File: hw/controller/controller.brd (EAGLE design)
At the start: 45 x 45 mm, 76 parts, among them J1 JST-PH3SMT_VERT, J2 JST-PH3SMT_VERT, Q1 TPN1R603PL, Q2 TPN1R603PL, Q3 TPN1R603PL, Q4 TPN1R603PL, Q5 TPN1R603PL, Q6 TPN1R603PL, U1 STM32F4R_64PIN, U2 DRV8323RS, U3 AS5147, U4 MAX13431E, X1 8.0MHz

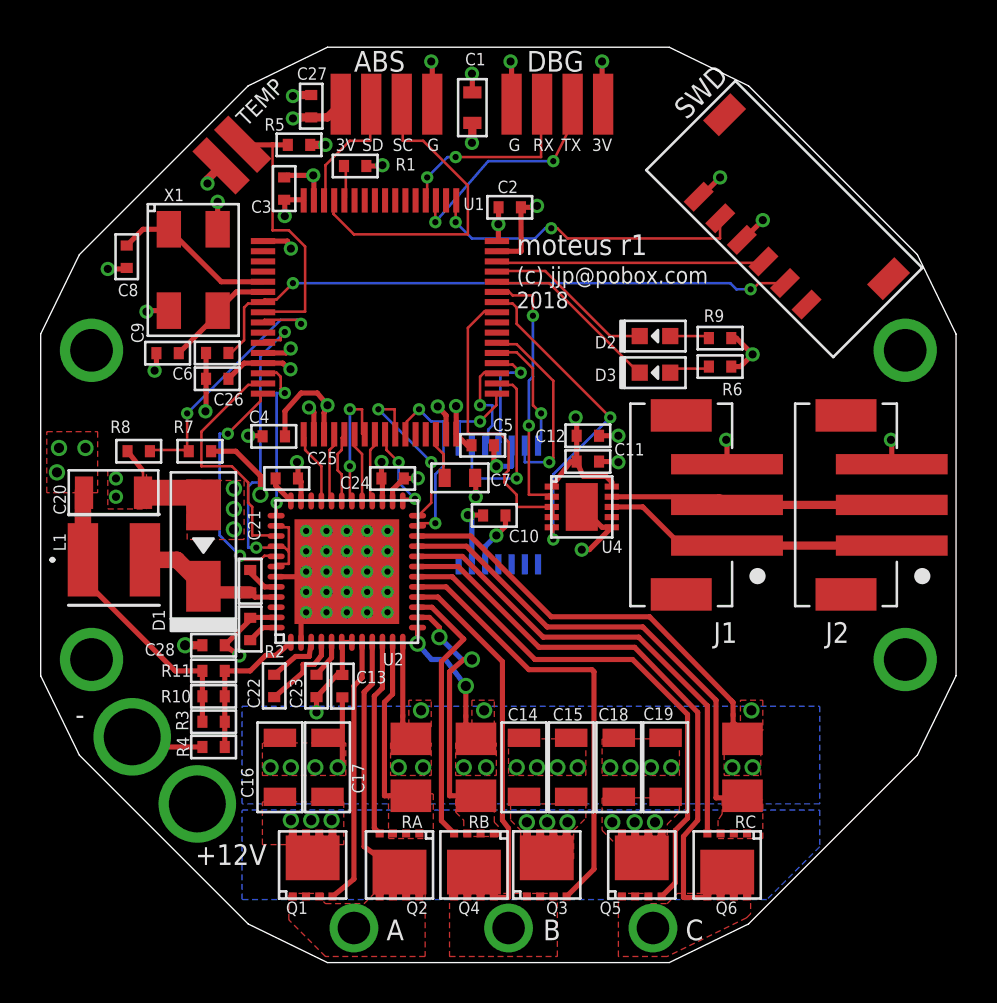
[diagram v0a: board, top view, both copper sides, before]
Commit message: More layout and schematic tweaks
 * Add a recommended 1uF bypass on the STM32 VDDA
 * Route VDRAIN on DRV8323 separately from VM
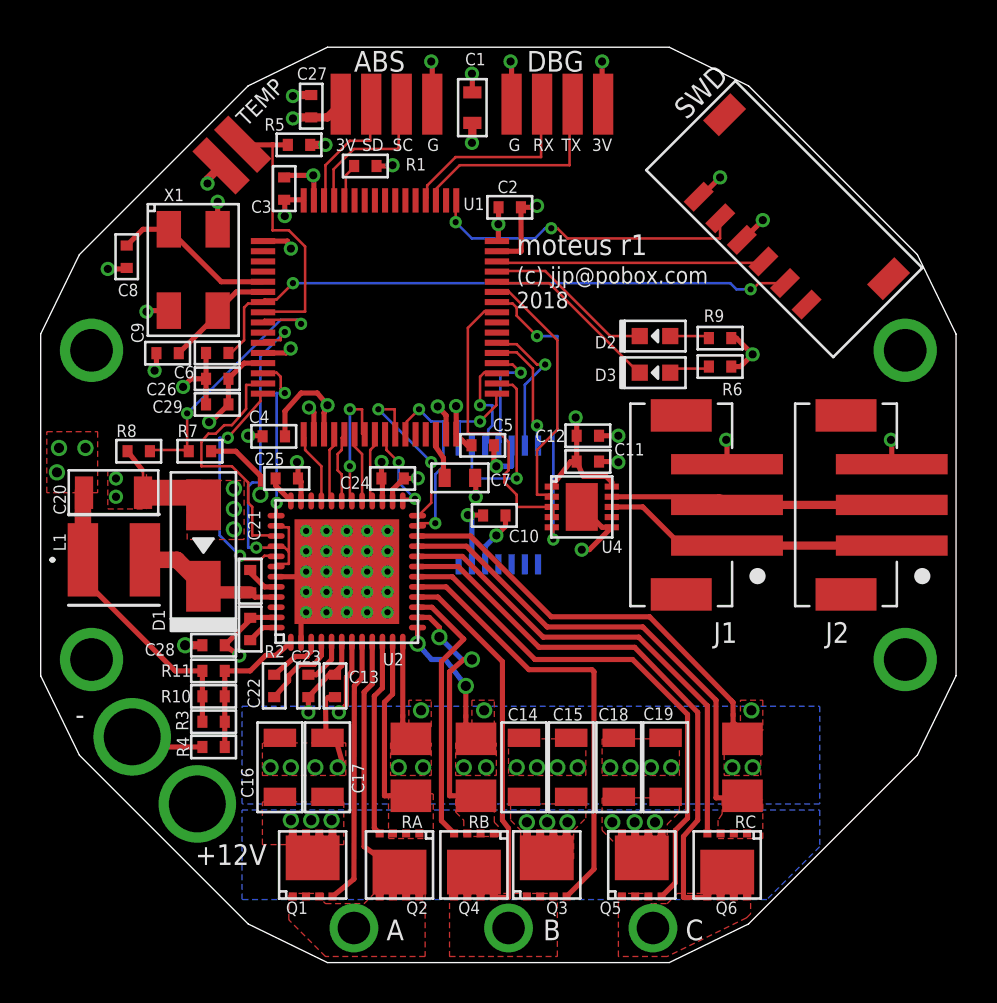
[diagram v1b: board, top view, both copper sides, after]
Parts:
- added C29: 1uF 35V, mfpassives:C0402
- moved R1 0.50 mm to (16.0, 39.2)
- moved C23 0.40 mm to (13.2, 13.6)
- moved C13 0.36 mm to (14.5, 13.6)
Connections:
- net +3V3: now also C29.P$1
- net GND: now also C29.P$2
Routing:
- net I2C_ABS_SCL: track 16.1 -> 7.50 mm
- net V+: track 16.6 -> 20.0 mm, vias 12 -> 13
- net AS5047_B: track 9.63 -> 7.19 mm
- net RS485_TX: track 16.2 -> 14.6 mm
- net +3V3: track 53.5 -> 54.6 mm
- net GND: track 51.1 -> 52.1 mm
- net V-: track 15.4 -> 16.3 mm
- net DEBUG_TX: track 11.4 -> 10.8 mm, vias 2 -> 0
- net DEBUG_RX: track 9.81 -> 9.58 mm, vias 2 -> 0
- net RS485_RX: track 12.9 -> 12.7 mm, vias 2 -> 0

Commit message: Fix a number of r1 errata
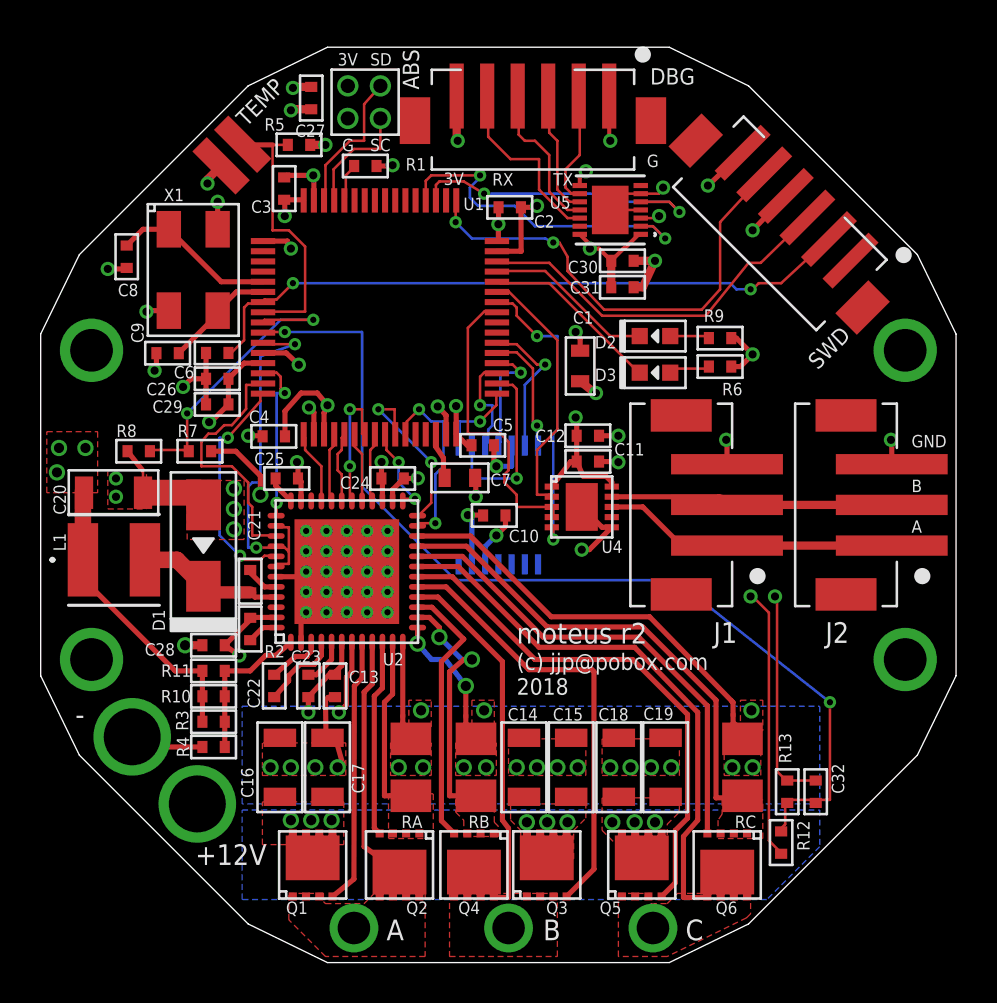
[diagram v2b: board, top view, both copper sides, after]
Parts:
- removed ABS: PAD4, controller:PAD15_4
- added ABS_3V, ABS_GND, ABS_SCL, ABS_SDA: PAD24AWG_PAD, controller:24AWG_PAD
- added C30: 1uF 35V, mfpassives:C0402
- added C31, C32: 0.1uF 50V, mfpassives:C0402
- added R12: 47k NTC, mfpassives:R0402
- added R13: 10k 1%, mfpassives:R0402
- added U5: MAX13433EETD+T, controller:21-0137I_T1433-1
- DBG: value PAD4 -> JST-ZH6SMT_VERT; device controller:PAD15_4 -> controller:JST_B6B-ZR-SM4-TF(LF)(SN)
- SWD: value JST-ZH6 -> JST-ZH6SMT_VERT; device controller:JST_S6B-ZR-SM4A-TF(LF)(SN) -> controller:JST_B6B-ZR-SM4-TF(LF)(SN)
- moved C1 13.8 mm to (26.5, 29.3)
- moved DBG 1.63 mm to (24.2, 41.1)
- moved SWD 1.56 mm to (36.1, 36.1), turned to 135 degrees
- moved C27 0.40 mm to (13.3, 42.5), turned to 270 degrees
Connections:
- net VTEMP renamed VTEMP_MOT
- new net DBG_A: DBG.5, U5.12
- new net DBG_B: DBG.4, U5.11
- new net DBG_Y: DBG.2, U5.9
- new net DBG_Z: DBG.3, U5.10
- new net VTEMP_FET: C32.P$1, R12.P$2, R13.P$1, U1.10
- net +3V3: now also ABS_3V.P$1, C30.P$1, C31.P$1, DBG.6, R12.P$1, U5.1, U5.14, U5.3; no longer ABS.1, DBG.1
- net DEBUG_RX: now also U5.2; no longer DBG.3
- net DEBUG_TX: now also U5.5; no longer DBG.2
- net GND: now also ABS_GND.P$1, C30.P$2, C31.P$2, C32.P$2, DBG.1, R13.P$2, U5.15, U5.4, U5.6, U5.8; no longer ABS.4, DBG.4
- net I2C_ABS_SCL: now also ABS_SCL.P$1; no longer ABS.3
- net I2C_ABS_SDA: now also ABS_SDA.P$1; no longer ABS.2
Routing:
- net VTEMP_FET: track 0.00 -> 48.2 mm, vias 0 -> 2
- net +3V3: track 54.6 -> 74.0 mm, vias 18 -> 21
- net GND: track 52.1 -> 71.0 mm, vias 30 -> 33
- net DBG_A: track 0.00 -> 9.06 mm
- net N$6: track 15.8 -> 23.3 mm
- net DBG_B: track 0.00 -> 7.51 mm
- net DEBUG_RX: track 9.58 -> 16.9 mm, vias 0 -> 2
- net DBG_Z: track 0.00 -> 6.14 mm
- net DBG_Y: track 0.00 -> 5.64 mm
- net N$7: track 13.1 -> 18.5 mm
- net DEBUG_TX: track 10.8 -> 15.4 mm, vias 0 -> 2
- net N$24: track 30.0 -> 33.0 mm
- net I2C_ABS_SCL: track 7.50 -> 5.75 mm
- net VBAT_SENSE: track 13.6 -> 14.5 mm
- net I2C_ABS_SDA: track 6.29 -> 7.15 mm
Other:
- board text added: "ABS"
- board text added: "GND"
- board text added: "moteus r2"
- board text removed: "moteus r1"

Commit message: Fix more errata in controller board
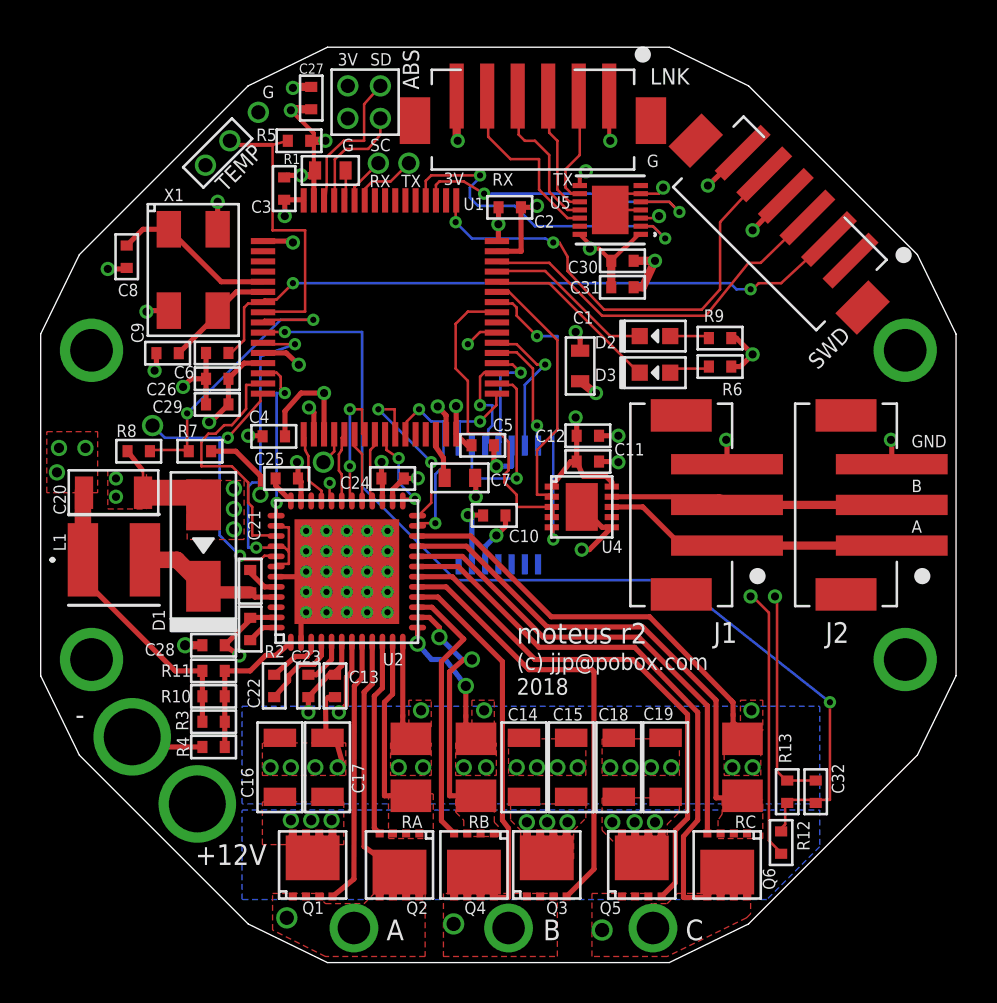
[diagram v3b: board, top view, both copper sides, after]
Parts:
- removed TEMP: PAD2, controller:PAD15_2
- added DA, DAC1, DB, DC, DGND, DRX, DTX, M3, TEMP1, TEMP2: PAD24AWG_PAD, controller:24AWG_PAD
- R1: device mfpassives:R0402 -> mfpassives:R0603
- moved R1 1.73 mm to (14.2, 38.9), turned to 0 degrees
- moved R5 0.20 mm to (12.7, 40.4)
- renumbered DBG to LNK
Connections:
- new net N$1: DAC1.P$1, U1.20
- new net N$2: DTX.P$1, U1.58
- new net N$3: DRX.P$1, U1.59
- net +3V3: now also TEMP1.P$1; no longer TEMP.1
- net DRV8323_CS: now also U1.39; no longer U1.20
- net GND: now also DGND.P$1
- net MOTOR3: now also M3.P$1
- net SHA: now also DA.P$1
- net SHB: now also DB.P$1
- net SHC: now also DC.P$1
- net VTEMP_MOT: now also TEMP2.P$1; no longer TEMP.2
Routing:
- net DRV8323_CS: track 3.40 -> 12.7 mm, vias 0 -> 2
- net GND: track 71.0 -> 74.7 mm, vias 33 -> 32
- net MOTOR3: track 11.6 -> 15.2 mm
- net N$2: track 0.00 -> 3.26 mm
- net N$3: track 0.00 -> 2.31 mm
- net N$1: track 0.00 -> 1.59 mm
- net +3V3: track 74.0 -> 72.8 mm, vias 21 -> 20
- net VTEMP_MOT: track 13.7 -> 14.8 mm
- net RS485_DIR: track 15.0 -> 16.0 mm
- net N$33: track 2.06 -> 1.49 mm
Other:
- board text added: "TEMP"

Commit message: More tweaks to controller board
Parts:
- removed R10, R3: 100k 1%, mfpassives:R0402
- R11: value 100k 1% -> 33k 1%
- moved R4 2.40 mm to (8.50, 13.0)
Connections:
- net +3V3: no longer R10.P$1, R3.P$1
- net N$8: no longer R10.P$2, R3.P$2
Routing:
- net +3V3: track 72.8 -> 70.3 mm
- net N$8: track 7.55 -> 5.15 mm
- net V-: track 16.3 -> 17.3 mm
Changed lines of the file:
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@@
 <attribute name="MF" value="Panasonic" x="10.3" y="16.4" size="1.778" layer="27" rot="R90" display="off"/>
 </element>
-<element name="R4" library="mfpassives" package="R0402" value="10k 1%" x="8.5" y="10.6" smashed="yes" rot="R180">
-<attribute name="TOLERANCE" value="" x="8.5" y="10.6" size="1.778" layer="27" rot="R180" display="off"/>
-<attribute name="MFG#" value="N/A" x="8.5" y="10.6" size="1.778" layer="27" rot="R180" display="off"/>
-<attribute name="VOLTAGE" value="" x="8.5" y="10.6" size="1.778" layer="27" rot="R180" display="off"/>
-<attribute name="WATTAGE" value="" x="8.5" y="10.6" size="1.778" layer="27" rot="R180" display="off"/>
-<attribute name="MPN" value="ERJ-2RKF1002X" x="8.5" y="10.6" size="1.778" layer="27" rot="R180" display="off"/>
-<attribute name="MF" value="Panasonic" x="8.5" y="10.6" size="1.778" layer="27" rot="R180" display="off"/>
-<attribute name="HOUSEPART" x="8.5" y="10.6" size="1.778" layer="27" rot="R180" display="off"/>
-<attribute name="POPULATE" value="1" x="8.5" y="10.6" size="1.778" layer="27" rot="R180" display="off"/>
-<attribute name="URL" x="8.5" y="10.6" size="1.778" layer="27" rot="R180" display="off"/>
-<attribute name="NAME" x="7.3" y="10.1" size="0.6096" layer="25" font="vector" ratio="10" rot="R90"/>
+<element name="R4" library="mfpassives" package="R0402" value="10k 1%" x="8.5" y="13" smashed="yes" rot="R180">
+<attribute name="TOLERANCE" value="" x="8.5" y="13" size="1.778" layer="27" rot="R180" display="off"/>
+<attribute name="MFG#" value="N/A" x="8.5" y="13" size="1.778" layer="27" rot="R180" display="off"/>
+<attribute name="VOLTAGE" value="" x="8.5" y="13" size="1.778" layer="27" rot="R180" display="off"/>
+<attribute name="WATTAGE" value="" x="8.5" y="13" size="1.778" layer="27" rot="R180" display="off"/>
+<attribute name="MPN" value="ERJ-2RKF1002X" x="8.5" y="13" size="1.778" layer="27" rot="R180" display="off"/>
+<attribute name="MF" value="Panasonic" x="8.5" y="13" size="1.778" layer="27" rot="R180" display="off"/>
+<attribute name="HOUSEPART" x="8.5" y="13" size="1.778" layer="27" rot="R180" display="off"/>
+<attribute name="POPULATE" value="1" x="8.5" y="13" size="1.778" layer="27" rot="R180" display="off"/>
+<attribute name="URL" x="8.5" y="13" size="1.778" layer="27" rot="R180" display="off"/>
+<attribute name="NAME" x="7.3" y="12.5" size="0.6096" layer="25" font="vector" ratio="10" rot="R90"/>
 </element>
 <element name="C21" library="mfpassives" package="C0402" value="0.1uF 50V" x="10.3" y="18.75" smashed="yes" rot="R270">
@@
 <attribute name="NAME" x="29.63" y="11.93" size="0.6096" layer="25" font="vector" ratio="10"/>
 </element>
-<element name="R3" library="mfpassives" package="R0402" value="100k 1%" x="8.5" y="11.84" smashed="yes">
-<attribute name="HOUSEPART" value="" x="8.5" y="11.84" size="1.016" layer="27" font="vector" ratio="10" display="off"/>
-<attribute name="TOLERANCE" value="" x="8.5" y="11.84" size="1.016" layer="27" font="vector" ratio="10" display="off"/>
-<attribute name="MPN" value="ERJ-2RKF1003X" x="8.5" y="11.84" size="1.016" layer="27" font="vector" ratio="10" display="off"/>
-<attribute name="POPULATE" value="1" x="8.5" y="11.84" size="1.016" layer="27" font="vector" ratio="10" display="off"/>
-<attribute name="VOLTAGE" value="" x="8.5" y="11.84" size="1.016" layer="27" font="vector" ratio="10" display="off"/>
-<attribute name="MF" value="Panasonic" x="8.5" y="11.84" size="1.016" layer="27" font="vector" ratio="10" display="off"/>
-<attribute name="URL" value="" x="8.5" y="11.84" size="1.016" layer="27" font="vector" ratio="10" display="off"/>
-<attribute name="WATTAGE" value="" x="8.5" y="11.84" size="1.016" layer="27" font="vector" ratio="10" display="off"/>
-<attribute name="NAME" x="7.26" y="11.4" size="0.6096" layer="25" font="vector" ratio="10" rot="R90"/>
-</element>
-<element name="R10" library="mfpassives" package="R0402" value="100k 1%" x="8.5" y="13.09" smashed="yes">
-<attribute name="HOUSEPART" value="" x="8.5" y="13.09" size="1.016" layer="27" font="vector" ratio="10" display="off"/>
-<attribute name="TOLERANCE" value="" x="8.5" y="13.09" size="1.016" layer="27" font="vector" ratio="10" display="off"/>
-<attribute name="MPN" value="ERJ-2RKF1003X" x="8.5" y="13.09" size="1.016" layer="27" font="vector" ratio="10" display="off"/>
-<attribute name="POPULATE" value="1" x="8.5" y="13.09" size="1.016" layer="27" font="vector" ratio="10" display="off"/>
-<attribute name="VOLTAGE" value="" x="8.5" y="13.09" size="1.016" layer="27" font="vector" ratio="10" display="off"/>
-<attribute name="MF" value="Panasonic" x="8.5" y="13.09" size="1.016" layer="27" font="vector" ratio="10" display="off"/>
-<attribute name="URL" value="" x="8.5" y="13.09" size="1.016" layer="27" font="vector" ratio="10" display="off"/>
-<attribute name="WATTAGE" value="" x="8.5" y="13.09" size="1.016" layer="27" font="vector" ratio="10" display="off"/>
-<attribute name="NAME" x="7.39" y="13.4" size="0.6096" layer="25" font="vector" ratio="10" rot="R180"/>
-</element>
-<element name="R11" library="mfpassives" package="R0402" value="100k 1%" x="8.5" y="14.34" smashed="yes">
+<element name="R11" library="mfpassives" package="R0402" value="33k 1%" x="8.5" y="14.34" smashed="yes">
 <attribute name="HOUSEPART" value="" x="8.5" y="14.34" size="1.016" layer="27" font="vector" ratio="10" display="off"/>
 <attribute name="TOLERANCE" value="" x="8.5" y="14.34" size="1.016" layer="27" font="vector" ratio="10" display="off"/>
-<attribute name="MPN" value="ERJ-2RKF1003X" x="8.5" y="14.34" size="1.016" layer="27" font="vector" ratio="10" display="off"/>
+<attribute name="MPN" value="ERJ-2RKF3302X" x="8.5" y="14.34" size="1.016" layer="27" font="vector" ratio="10" display="off"/>
 <attribute name="POPULATE" value="1" x="8.5" y="14.34" size="1.016" layer="27" font="vector" ratio="10" display="off"/>
 <attribute name="VOLTAGE" value="" x="8.5" y="14.34" size="1.016" layer="27" font="vector" ratio="10" display="off"/>
@@
 <attribute name="MANUFACTURER_PART_NUMBER" value="MAX13433EETD+T" x="28" y="37" size="0.8" layer="27" rot="R180" display="off"/>
 <attribute name="NAME" x="25.0234" y="37.065" size="0.6096" layer="25" ratio="10" rot="SR0"/>
+<attribute name="MPN" value="MAX13433EETD+T" x="28" y="37" size="1.778" layer="27" rot="R180" display="off"/>
+<attribute name="MF" value="Maxim" x="28" y="37" size="1.778" layer="27" rot="R180" display="off"/>
+<attribute name="POPULATE" value="1" x="28" y="37" size="1.778" layer="27" rot="R180" display="off"/>
 </element>
 <element name="LNK" library="controller" package="JST_B6B-ZR-SM4-TF(LF)(SN)" value="JST-ZH6SMT_VERT" x="24.2" y="41.1" smashed="yes" rot="R180">
@@
 <contactref element="C20" pad="P$1"/>
 <contactref element="R11" pad="P$1"/>
-<contactref element="R10" pad="P$1"/>
-<contactref element="R3" pad="P$1"/>
-<wire x1="7.95" y1="11.84" x2="7.95" y2="13.09" width="0.254" layer="1"/>
-<wire x1="7.95" y1="13.09" x2="7.95" y2="14.34" width="0.254" layer="1"/>
 <wire x1="7.95" y1="14.34" x2="6.61" y2="14.34" width="0.254" layer="1"/>
 <wire x1="6.61" y1="14.34" x2="2.076" y2="18.874" width="0.254" layer="1"/>
@@
 <via x="7.1" y="15.6" extent="1-16" drill="0.5"/>
 <wire x1="7.95" y1="15.6" x2="7.1" y2="15.6" width="0.4064" layer="1"/>
-<wire x1="7.95" y1="10.6" x2="5.4" y2="10.6" width="0.254" layer="1"/>
-<wire x1="5.4" y1="10.6" x2="4.5" y2="11.1" width="0.254" layer="1"/>
+<wire x1="7.95" y1="13" x2="5.5" y2="13" width="0.254" layer="1"/>
+<wire x1="5.5" y1="13" x2="4.5" y2="11.1" width="0.254" layer="1"/>
 <wire x1="18.2" y1="11" x2="17.8" y2="11.4" width="0.254" layer="1"/>
 <wire x1="17.8" y1="11.4" x2="17.8" y2="11.823" width="0.254" layer="1"/>
@@
 <wire x1="11.555" y1="15.1" x2="11.06" y2="15.1" width="0.254" layer="1"/>
 <contactref element="R11" pad="P$2"/>
-<contactref element="R10" pad="P$2"/>
-<contactref element="R3" pad="P$2"/>
 <wire x1="11.06" y1="15.1" x2="10.3" y2="14.34" width="0.254" layer="1"/>
 <wire x1="10.3" y1="14.34" x2="9.05" y2="14.34" width="0.254" layer="1"/>
-<wire x1="9.05" y1="14.34" x2="9.05" y2="13.09" width="0.254" layer="1"/>
-<wire x1="9.05" y1="13.09" x2="9.05" y2="11.84" width="0.254" layer="1"/>
-<wire x1="9.05" y1="11.84" x2="9.05" y2="10.6" width="0.254" layer="1"/>
+<wire x1="9.05" y1="13" x2="9.05" y2="14.34" width="0.3048" layer="1"/>
 </signal>
 <signal name="N$11">
